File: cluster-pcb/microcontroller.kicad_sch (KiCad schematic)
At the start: 2 parts

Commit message: Finalize layout
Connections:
- net ENABLE_TX_0: now also A401.20 (I2C1-SCL/SPI1-TX/GP15); no longer A401.1 (UART0-TX/I2C0-SDA/SPI0-RX/GP0)
- net ENABLE_TX_1: now also A401.17 (UART0-RX/I2C0-SCL/SPI1-CS/GP13); no longer A401.4 (I2C1-SDA/SPI0-SCK/GP2)
- net ENABLE_TX_2: now also A401.15 (I2C1-SCL/SPI1-TX/GP11); no longer A401.9 (I2C1-SDA/SPI0-SCK/GP6)
- net ENABLE_TX_3: now also A401.12 (UART1-RX/I2C0-SCL/SPI1-CS/GP9); no longer A401.11 (UART1-TX/I2C0-SDA/SPI1-RX/GP8)
- net ENABLE_TX_4: now also A401.10 (I2C1-SCL/SPI0-TX/GP7); no longer A401.14 (I2C1-SDA/SPI1-SCK/GP10)
- net ENABLE_TX_5: now also A401.5 (I2C1-SCL/SPI0-TX/GP3); no longer A401.16 (UART0-TX/I2C0-SDA/SPI1-RX/GP12)
- net ENABLE_TX_6: now also A401.2 (UART0-RX/I2C0-SCL/SPI0-CS/GP1); no longer A401.19 (I2C1-SDA/SPI1-SCK/GP14)
- net ~{ENABLE_RX_0}: now also A401.19 (I2C1-SDA/SPI1-SCK/GP14); no longer A401.2 (UART0-RX/I2C0-SCL/SPI0-CS/GP1)
- net ~{ENABLE_RX_1}: now also A401.16 (UART0-TX/I2C0-SDA/SPI1-RX/GP12); no longer A401.5 (I2C1-SCL/SPI0-TX/GP3)
- net ~{ENABLE_RX_2}: now also A401.14 (I2C1-SDA/SPI1-SCK/GP10); no longer A401.10 (I2C1-SCL/SPI0-TX/GP7)
- net ~{ENABLE_RX_3}: now also A401.11 (UART1-TX/I2C0-SDA/SPI1-RX/GP8); no longer A401.12 (UART1-RX/I2C0-SCL/SPI1-CS/GP9)
- net ~{ENABLE_RX_4}: now also A401.9 (I2C1-SDA/SPI0-SCK/GP6); no longer A401.15 (I2C1-SCL/SPI1-TX/GP11)
- net ~{ENABLE_RX_5}: now also A401.4 (I2C1-SDA/SPI0-SCK/GP2); no longer A401.17 (UART0-RX/I2C0-SCL/SPI1-CS/GP13)
- net ~{ENABLE_RX_6}: now also A401.1 (UART0-TX/I2C0-SDA/SPI0-RX/GP0); no longer A401.20 (I2C1-SCL/SPI1-TX/GP15)
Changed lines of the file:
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@@
   (title_block
     (title "cluster-pcb")
-    (date "2024-07-18")
+    (date "2024-07-26")
     (rev "1.0")
     (company "Howard Hughes Medical Institute")
@@
     (effects (font (size 1.27 1.27)) (justify left))
   )
-  (hierarchical_label "~{ENABLE_RX_0}" (shape output) (at 91.44 71.12 180) (fields_autoplaced)
+  (hierarchical_label "~{ENABLE_RX_6}" (shape output) (at 91.44 68.58 180) (fields_autoplaced)
     (effects (font (size 1.27 1.27)) (justify right))
   )
-  (hierarchical_label "~{ENABLE_RX_6}" (shape output) (at 91.44 116.84 180) (fields_autoplaced)
+  (hierarchical_label "~{ENABLE_RX_0}" (shape output) (at 91.44 114.3 180) (fields_autoplaced)
     (effects (font (size 1.27 1.27)) (justify right))
   )
-  (hierarchical_label "ENABLE_TX_4" (shape output) (at 91.44 101.6 180) (fields_autoplaced)
+  (hierarchical_label "ENABLE_TX_2" (shape output) (at 91.44 104.14 180) (fields_autoplaced)
     (effects (font (size 1.27 1.27)) (justify right))
   )
@@
     (effects (font (size 1.27 1.27)) (justify right))
   )
-  (hierarchical_label "ENABLE_TX_0" (shape output) (at 91.44 68.58 180) (fields_autoplaced)
+  (hierarchical_label "ENABLE_TX_6" (shape output) (at 91.44 71.12 180) (fields_autoplaced)
     (effects (font (size 1.27 1.27)) (justify right))
   )
-  (hierarchical_label "~{ENABLE_RX_3}" (shape output) (at 91.44 96.52 180) (fields_autoplaced)
+  (hierarchical_label "~{ENABLE_RX_3}" (shape output) (at 91.44 93.98 180) (fields_autoplaced)
     (effects (font (size 1.27 1.27)) (justify right))
   )
@@
     (effects (font (size 1.27 1.27)) (justify right))
   )
-  (hierarchical_label "ENABLE_TX_5" (shape output) (at 91.44 106.68 180) (fields_autoplaced)
+  (hierarchical_label "ENABLE_TX_1" (shape output) (at 91.44 109.22 180) (fields_autoplaced)
     (effects (font (size 1.27 1.27)) (justify right))
   )
-  (hierarchical_label "ENABLE_TX_6" (shape output) (at 91.44 114.3 180) (fields_autoplaced)
+  (hierarchical_label "ENABLE_TX_0" (shape output) (at 91.44 116.84 180) (fields_autoplaced)
     (effects (font (size 1.27 1.27)) (justify right))
   )
-  (hierarchical_label "ENABLE_TX_3" (shape output) (at 91.44 93.98 180) (fields_autoplaced)
+  (hierarchical_label "ENABLE_TX_3" (shape output) (at 91.44 96.52 180) (fields_autoplaced)
     (effects (font (size 1.27 1.27)) (justify right))
   )
-  (hierarchical_label "ENABLE_TX_1" (shape output) (at 91.44 76.2 180) (fields_autoplaced)
+  (hierarchical_label "ENABLE_TX_5" (shape output) (at 91.44 78.74 180) (fields_autoplaced)
     (effects (font (size 1.27 1.27)) (justify right))
   )
-  (hierarchical_label "~{ENABLE_RX_2}" (shape output) (at 91.44 91.44 180) (fields_autoplaced)
+  (hierarchical_label "~{ENABLE_RX_4}" (shape output) (at 91.44 88.9 180) (fields_autoplaced)
     (effects (font (size 1.27 1.27)) (justify right))
   )
-  (hierarchical_label "ENABLE_TX_2" (shape output) (at 91.44 88.9 180) (fields_autoplaced)
+  (hierarchical_label "ENABLE_TX_4" (shape output) (at 91.44 91.44 180) (fields_autoplaced)
     (effects (font (size 1.27 1.27)) (justify right))
   )
@@
     (effects (font (size 1.27 1.27)) (justify right))
   )
-  (hierarchical_label "~{ENABLE_RX_5}" (shape output) (at 91.44 109.22 180) (fields_autoplaced)
+  (hierarchical_label "~{ENABLE_RX_1}" (shape output) (at 91.44 106.68 180) (fields_autoplaced)
     (effects (font (size 1.27 1.27)) (justify right))
   )
@@
     (effects (font (size 1.27 1.27)) (justify right))
   )
-  (hierarchical_label "~{ENABLE_RX_1}" (shape output) (at 91.44 78.74 180) (fields_autoplaced)
+  (hierarchical_label "~{ENABLE_RX_5}" (shape output) (at 91.44 76.2 180) (fields_autoplaced)
     (effects (font (size 1.27 1.27)) (justify right))
   )
-  (hierarchical_label "~{ENABLE_RX_4}" (shape output) (at 91.44 104.14 180) (fields_autoplaced)
+  (hierarchical_label "~{ENABLE_RX_2}" (shape output) (at 91.44 101.6 180) (fields_autoplaced)
     (effects (font (size 1.27 1.27)) (justify right))
   )

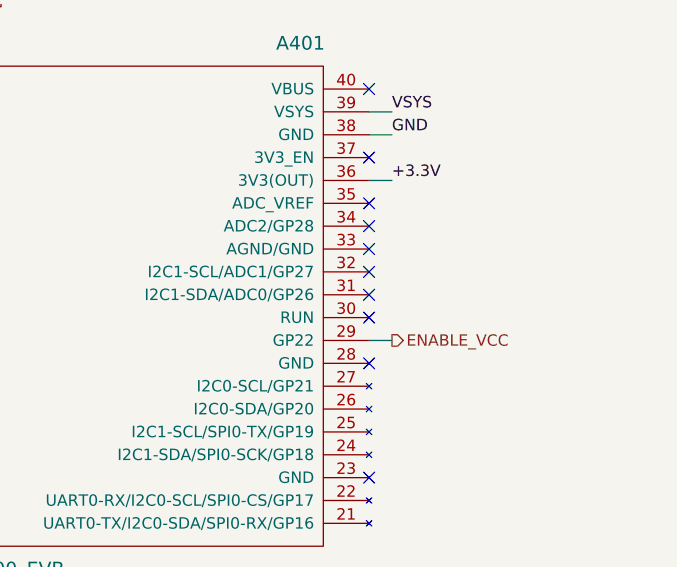
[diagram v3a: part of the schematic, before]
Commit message: Add address
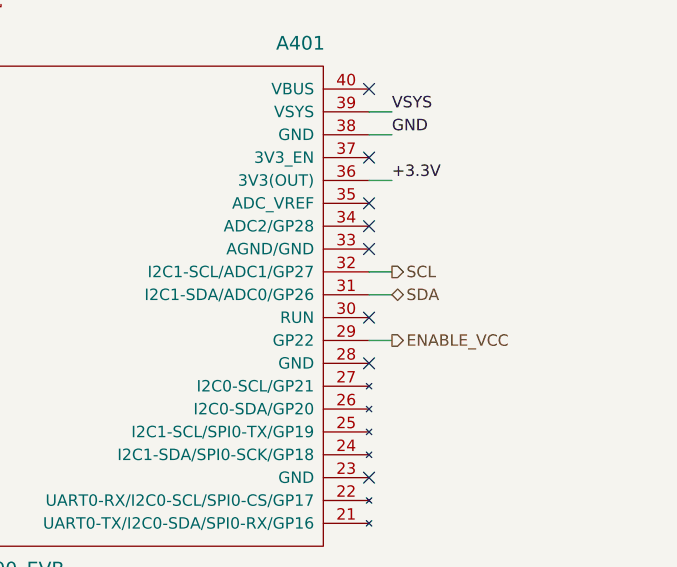
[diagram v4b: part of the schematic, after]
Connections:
- net SDA: now reaches A401.31 (I2C1-SDA/ADC0/GP26)
- net SCL: now reaches A401.32 (I2C1-SCL/ADC1/GP27)
- no-connect marks 14 -> 12
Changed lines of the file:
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@@
     (title "cluster-pcb")
     (date "2024-08-26")
-    (rev "1.1")
+    (rev "1.2")
     (company "Howard Hughes Medical Institute")
   )
@@
   (no_connect (at 180.34 99.06))
   (no_connect (at 93.98 86.36))
-  (no_connect (at 180.34 91.44))
   (no_connect (at 180.34 68.58))
   (no_connect (at 180.34 86.36))
@@
   (no_connect (at 180.34 76.2))
   (no_connect (at 93.98 99.06))
-  (no_connect (at 180.34 88.9))
   (no_connect (at 93.98 73.66))
   (no_connect (at 93.98 111.76))
@@
   )
   (wire (pts (xy 91.44 71.12) (xy 93.98 71.12))
+    (stroke (width 0) (type default))
+  )
+  (wire (pts (xy 180.34 91.44) (xy 182.88 91.44))
     (stroke (width 0) (type default))
   )
@@
   )
   (wire (pts (xy 54.61 46.99) (xy 57.15 46.99))
+    (stroke (width 0) (type default))
+  )
+  (wire (pts (xy 180.34 88.9) (xy 182.88 88.9))
     (stroke (width 0) (type default))
   )
@@
     (effects (font (size 1.27 1.27)) (justify right))
   )
+  (hierarchical_label "SDA" (shape bidirectional) (at 182.88 91.44 0) (fields_autoplaced)
+    (effects (font (size 1.27 1.27)) (justify left))
+  )
   (hierarchical_label "~{ENABLE_RX_4}" (shape output) (at 91.44 88.9 180) (fields_autoplaced)
     (effects (font (size 1.27 1.27)) (justify right))
   )
+  (hierarchical_label "SCL" (shape output) (at 182.88 88.9 0) (fields_autoplaced)
+    (effects (font (size 1.27 1.27)) (justify left))
+  )
   (hierarchical_label "ENABLE_TX_4" (shape output) (at 91.44 91.44 180) (fields_autoplaced)

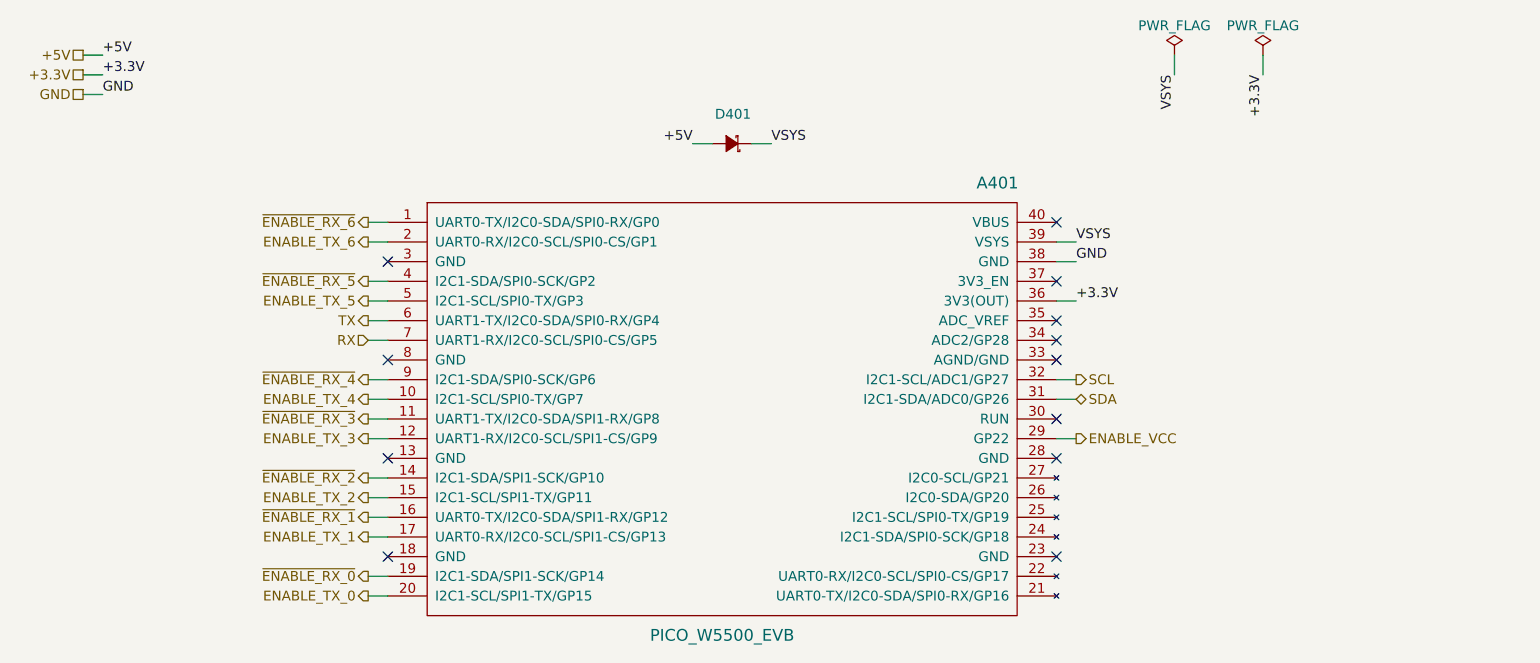
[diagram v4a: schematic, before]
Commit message: Add i2c pullups
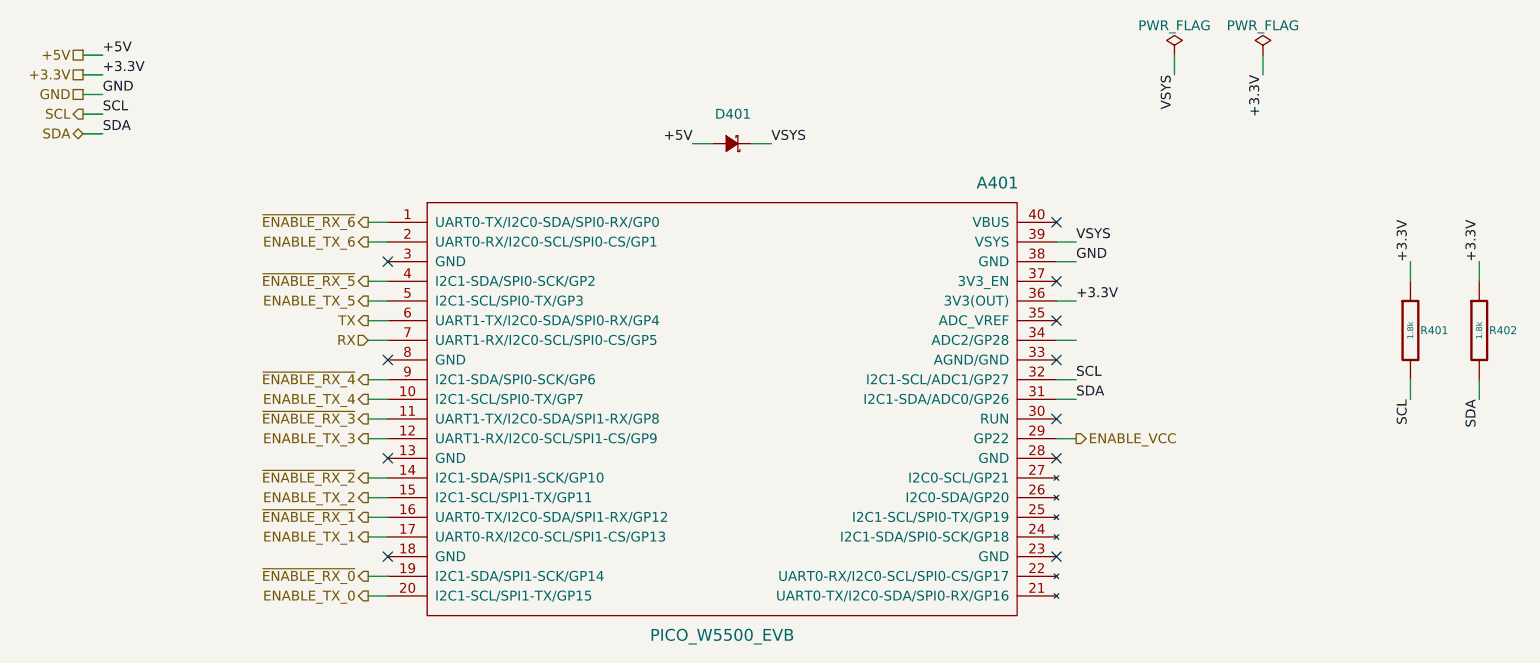
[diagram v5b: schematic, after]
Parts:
- added R401, R402: 1.8k, Janelia:R_0402_1005Metric, symbol Janelia:R_1.8k_0402
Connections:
- net +3.3V: now also R401.1, R402.1
- net SCL: now also R401.2
- net SDA: now also R402.2
- no-connect marks 12 -> 11
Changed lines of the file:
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@@
   (no_connect (at 93.98 73.66))
   (no_connect (at 93.98 111.76))
-  (no_connect (at 180.34 83.82))
   (wire (pts (xy 207.01 46.99) (xy 207.01 49.53))
     (stroke (width 0) (type default))
   )
+  (wire (pts (xy 226.06 88.9) (xy 226.06 91.44))
+    (stroke (width 0) (type default))
+  )
+  (wire (pts (xy 226.06 76.2) (xy 226.06 73.66))
+    (stroke (width 0) (type default))
+  )
   (wire (pts (xy 91.44 109.22) (xy 93.98 109.22))
     (stroke (width 0) (type default))
@@
     (stroke (width 0) (type default))
   )
+  (wire (pts (xy 54.61 57.15) (xy 57.15 57.15))
+    (stroke (width 0) (type default))
+  )
   (wire (pts (xy 180.34 96.52) (xy 182.88 96.52))
     (stroke (width 0) (type default))
@@
     (stroke (width 0) (type default))
   )
+  (wire (pts (xy 234.95 88.9) (xy 234.95 91.44))
+    (stroke (width 0) (type default))
+  )
   (wire (pts (xy 91.44 81.28) (xy 93.98 81.28))
     (stroke (width 0) (type default))
@@
     (stroke (width 0) (type default))
   )
+  (wire (pts (xy 54.61 54.61) (xy 57.15 54.61))
+    (stroke (width 0) (type default))
+  )
   (wire (pts (xy 91.44 101.6) (xy 93.98 101.6))
     (stroke (width 0) (type default))
@@
     (stroke (width 0) (type default))
   )
+  (wire (pts (xy 180.34 83.82) (xy 182.88 83.82))
+    (stroke (width 0) (type default))
+  )
   (wire (pts (xy 180.34 88.9) (xy 182.88 88.9))
     (stroke (width 0) (type default))
   )
   (wire (pts (xy 180.34 71.12) (xy 182.88 71.12))
+    (stroke (width 0) (type default))
+  )
+  (wire (pts (xy 234.95 76.2) (xy 234.95 73.66))
     (stroke (width 0) (type default))
   )
@@
     (effects (font (size 1.27 1.27)) (justify right bottom))
   )
+  (label "+3.3V" (at 226.06 73.66 90) (fields_autoplaced)
+    (effects (font (size 1.27 1.27)) (justify left bottom))
+  )
+  (label "SDA" (at 234.95 91.44 270) (fields_autoplaced)
+    (effects (font (size 1.27 1.27)) (justify right bottom))
+  )
+  (label "SCL" (at 182.88 88.9 0) (fields_autoplaced)
+    (effects (font (size 1.27 1.27)) (justify left bottom))
+  )
   (label "VSYS" (at 182.88 71.12 0) (fields_autoplaced)
+    (effects (font (size 1.27 1.27)) (justify left bottom))
+  )
+  (label "SDA" (at 57.15 57.15 0) (fields_autoplaced)
+    (effects (font (size 1.27 1.27)) (justify left bottom))
+  )
+  (label "SDA" (at 182.88 91.44 0) (fields_autoplaced)
     (effects (font (size 1.27 1.27)) (justify left bottom))
   )
@@
     (effects (font (size 1.27 1.27)) (justify left bottom))
   )
+  (label "SCL" (at 57.15 54.61 0) (fields_autoplaced)
+    (effects (font (size 1.27 1.27)) (justify left bottom))
+  )
+  (label "SCL" (at 226.06 91.44 270) (fields_autoplaced)
+    (effects (font (size 1.27 1.27)) (justify right bottom))
+  )
+  (label "+3.3V" (at 234.95 73.66 90) (fields_autoplaced)
+    (effects (font (size 1.27 1.27)) (justify left bottom))
+  )
   (label "GND" (at 182.88 73.66 0) (fields_autoplaced)
     (effects (font (size 1.27 1.27)) (justify left bottom))
@@
     (effects (font (size 1.27 1.27)) (justify right))
   )
-  (hierarchical_label "SDA" (shape bidirectional) (at 182.88 91.44 0) (fields_autoplaced)
-    (effects (font (size 1.27 1.27)) (justify left))
+  (hierarchical_label "SDA" (shape bidirectional) (at 54.61 57.15 180) (fields_autoplaced)
+    (effects (font (size 1.27 1.27)) (justify right))
   )
   (hierarchical_label "~{ENABLE_RX_4}" (shape output) (at 91.44 88.9 180) (fields_autoplaced)
     (effects (font (size 1.27 1.27)) (justify right))
   )
-  (hierarchical_label "SCL" (shape output) (at 182.88 88.9 0) (fields_autoplaced)
-    (effects (font (size 1.27 1.27)) (justify left))
+  (hierarchical_label "SCL" (shape output) (at 54.61 54.61 180) (fields_autoplaced)
+    (effects (font (size 1.27 1.27)) (justify right))
   )
   (hierarchical_label "ENABLE_TX_4" (shape output) (at 91.44 91.44 180) (fields_autoplaced)
@@
     )
   )
+  (symbol (lib_id "Janelia:R_1.8k_0402") (at 234.95 82.55 0) (unit 1)
+    (in_bom yes) (on_board yes) (dnp no)
+    (property "Reference" "R402" (at 236.22 82.55 0)
+      (effects (font (size 1.016 1.016)) (justify left))
+    )
+    (property "Value" "1.8k" (at 234.95 82.55 90) (do_not_autoplace)
+      (effects (font (size 0.762 0.762)))
+    )
+    (property "Footprint" "Janelia:R_0402_1005Metric" (at 233.172 82.55 90)
+      (effects (font (size 0.762 0.762)) hide)
+    )
+    (property "Datasheet" "" (at 236.982 82.55 90)
+      (effects (font (size 0.762 0.762)))
+    )
+    (property "Vendor" "JLCPCB" (at 239.522 80.01 90)
+      (effects (font (size 1.524 1.524)) hide)
+    )
+    (property "Vendor Part Number" "C409855" (at 242.062 77.47 90)
+      (effects (font (size 1.524 1.524)) hide)
+    )
+    (property "Synopsis" "RES SMD 1.8K OHM 5% 100mW" (at 244.602 74.93 90)
+      (effects (font (size 1.524 1.524)) hide)
+    )
+    (property "Package" "0402" (at 234.95 82.55 0)
+      (effects (font (size 1.27 1.27)) hide)
+    )
+    (property "Manufacturer" "PANASONIC" (at 234.95 82.55 0)
+      (effects (font (size 1.27 1.27)) hide)
+    )
+    (property "Manufacturer Part Number" "ERJ2GEJ182X" (at 234.95 82.55 0)
+      (effects (font (size 1.27 1.27)) hide)
+    )
+    (property "LCSC" "C409855" (at 234.95 82.55 0)
+      (effects (font (size 1.27 1.27)) hide)
+    )
+    (pin "2")
+    (pin "1")
+    (instances
+      (project "cluster-pcb"
+        (path "/df2b2e89-e055-4140-95de-f1df723db034/90ad6836-1738-4b32-a341-0a0b169f4662"
+          (reference "R402") (unit 1)
+        )
+      )
+    )
+  )
   (symbol (lib_id "power:PWR_FLAG") (at 195.58 46.99 0) (unit 1)
     (in_bom yes) (on_board yes) (dnp no)
@@
         )
       )
+    )
+  )
+  (symbol (lib_id "Janelia:R_1.8k_0402") (at 226.06 82.55 0) (unit 1)
+    (in_bom yes) (on_board yes) (dnp no)
+    (property "Reference" "R401" (at 227.33 82.55 0)
+      (effects (font (size 1.016 1.016)) (justify left))
+    )
+    (property "Value" "1.8k" (at 226.06 82.55 90) (do_not_autoplace)
+      (effects (font (size 0.762 0.762)))
+    )
+    (property "Footprint" "Janelia:R_0402_1005Metric" (at 224.282 82.55 90)
+      (effects (font (size 0.762 0.762)) hide)
+    )
+    (property "Datasheet" "" (at 228.092 82.55 90)
+      (effects (font (size 0.762 0.762)))
+    )
+    (property "Vendor" "JLCPCB" (at 230.632 80.01 90)
+      (effects (font (size 1.524 1.524)) hide)
+    )
+    (property "Vendor Part Number" "C409855" (at 233.172 77.47 90)
+      (effects (font (size 1.524 1.524)) hide)
+    )
+    (property "Synopsis" "RES SMD 1.8K OHM 5% 100mW" (at 235.712 74.93 90)
+      (effects (font (size 1.524 1.524)) hide)
+    )
+    (property "Package" "0402" (at 226.06 82.55 0)
+      (effects (font (size 1.27 1.27)) hide)
+    )
+    (property "Manufacturer" "PANASONIC" (at 226.06 82.55 0)
+      (effects (font (size 1.27 1.27)) hide)
+    )
+    (property "Manufacturer Part Number" "ERJ2GEJ182X" (at 226.06 82.55 0)
+      (effects (font (size 1.27 1.27)) hide)
+    )
+    (property "LCSC" "C409855" (at 226.06 82.55 0)
+      (effects (font (size 1.27 1.27)) hide)
+    )
+    (pin "2")
+    (pin "1")
+    (instances
+      (project "cluster-pcb"
+        (path "/df2b2e89-e055-4140-95de-f1df723db034/90ad6836-1738-4b32-a341-0a0b169f4662"
+          (reference "R401") (unit 1)
+        )
+      )

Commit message: Update schematic
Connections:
- net AUDIO: now reaches A401.34 (ADC2/GP28)
- net ENABLE_TX_0 renamed ENABLE_TXRX_0
- net ENABLE_TX_1 renamed ENABLE_TXRX_2
- net ENABLE_TX_2 renamed ENABLE_TXRX_4
- net ENABLE_TX_3 renamed ENABLE_TXRX_6
- net ENABLE_TX_4 renamed MUX_ADDRESS_1
- net ENABLE_TX_5: no longer names the net of A401.5 (I2C1-SCL/SPI0-TX/GP3)
- net ENABLE_TX_6: no longer names the net of A401.2 (UART0-RX/I2C0-SCL/SPI0-CS/GP1)
- net ENABLE_VCC renamed ENABLE_POWER
- net ~{ENABLE_RX_0} renamed ENABLE_TXRX_1
- net ~{ENABLE_RX_1} renamed ENABLE_TXRX_3
- net ~{ENABLE_RX_2} renamed ENABLE_TXRX_5
- net ~{ENABLE_RX_3} renamed MUX_ADDRESS_0
- net ~{ENABLE_RX_4} renamed MUX_ADDRESS_2
- net ~{ENABLE_RX_5}: no longer names the net of A401.4 (I2C1-SDA/SPI0-SCK/GP2)
- net ~{ENABLE_RX_6}: no longer names the net of A401.1 (UART0-TX/I2C0-SDA/SPI0-RX/GP0)
- no-connect marks 11 -> 15
